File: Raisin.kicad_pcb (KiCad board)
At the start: 2 copper layers, 6 parts, among them U1 ATMEGA328P-AU, U10 L78L06_TO92, U5 LD1117S33TR_SOT223, U6 L78L05_TO92, U7 FSA3157L6X, U8 AD5171

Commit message: bad pcb layout
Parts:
- removed U8: AD5171, TO_SOT_Packages_SMD:SOT-23-8_Handsoldering
- added C1: 100nF, raisin:C_1206_0603, F.Cu at (102.5, 135.8)
- added C10: 10uF, Capacitors_ThroughHole:CP_Radial_D4.0mm_P2.00mm, B.Cu at (150.7, 99.7)
- added C11: 10nF, raisin:C_1206_0603, F.Cu at (76.9, 103.7)
- added C12: 10nF, raisin:C_1206_0603, F.Cu at (73.0, 79.8)
- added C13: 100nF, raisin:C_1206_0603, F.Cu at (75.5, 128.3)
- added C14: 10nF, raisin:C_1206_0603, F.Cu at (70.9, 110.0)
- added C15: 100nF, raisin:C_1206_0603, F.Cu at (83.4, 109.3)
- added C16: 10nF, raisin:C_1206_0603, F.Cu at (68.0, 95.9)
- added C17: 100nF, raisin:C_1206_0603, F.Cu at (68.2, 120.2)
- added C19: 100nF, raisin:C_1206_0603, F.Cu at (79.2, 120.3)
- added C2: 100nF, raisin:C_1206_0603, F.Cu at (108.5, 119.2)
- added C20: 220nF, raisin:C_1206_0603, F.Cu at (100.2, 102.6)
- added C21: 220nF, raisin:C_1206_0603, F.Cu at (105.3, 102.6)
- added C22: 220nF, raisin:C_1206_0603, F.Cu at (110.3, 102.6)
- added C23: 220nF, raisin:C_1206_0603, F.Cu at (115.4, 102.6)
- added C24: 10nF, raisin:C_1206_0603, F.Cu at (83.5, 86.7)
- added C25: 100nF, raisin:C_1206_0603, F.Cu at (80.0, 96.0)
- added C26: 220nF, raisin:C_1206_0603, F.Cu at (120.5, 102.6)
- added C27: 100nF, raisin:C_1206_0603, F.Cu at (79.2, 87.0)
- added C28: 220nF, raisin:C_1206_0603, F.Cu at (125.5, 102.6)
- added C29: 33uF, Capacitors_ThroughHole:CP_Radial_D6.3mm_P2.50mm, B.Cu at (85.0, 98.0)
- added C3: 22pF, raisin:C_1206_0603, F.Cu at (128.7, 132.4)
- added C30: 220nF, raisin:C_1206_0603, F.Cu at (130.6, 102.6)
- added C31: 100nF, raisin:C_1206_0603, F.Cu at (122.9, 76.5)
- added C32: 33uF, Capacitors_ThroughHole:CP_Radial_D6.3mm_P2.50mm, B.Cu at (125.2, 57.8)
- added C33: 100nF, raisin:C_1206_0603, F.Cu at (122.1, 56.5)
- added C34: 1uF, Capacitors_ThroughHole:CP_Radial_D4.0mm_P2.00mm, B.Cu at (134.3, 62.2)
- added C35: 100nF, raisin:C_1206_0603, F.Cu at (140.2, 97.0)
- added C36: 100nF, raisin:C_1206_0603, F.Cu at (117.2, 81.6)
- added C37: 75*, raisin:C_1206_0603, F.Cu at (125.8, 87.5)
- added C38: 100nF, raisin:C_1206_0603, F.Cu at (111.0, 91.6)
- added C39: 10nF, raisin:C_1206_0603, F.Cu at (85.4, 76.3)
- added C4: 22pF, raisin:C_1206_0603, F.Cu at (116.6, 132.4)
- added C40: 10nF, raisin:C_1206_0603, F.Cu at (130.7, 88.9)
- added C41: 10nF, raisin:C_1206_0603, F.Cu at (76.0, 52.9)
- added C42: 100nF, raisin:C_1206_0603, F.Cu at (112.4, 62.2)
- added C43: 1uF, Capacitors_ThroughHole:CP_Radial_D4.0mm_P2.00mm, B.Cu at (126.5, 48.1)
- added C44: 270, raisin:C_1206_0603, F.Cu at (68.8, 54.0)
- added C45: 27, raisin:C_1206_0603, F.Cu at (75.5, 59.0)
- added C46: 33, raisin:C_1206_0603, F.Cu at (69.5, 59.0)
- added C47: 100nF, raisin:C_1206_0603, F.Cu at (101.9, 70.3)
- added C48: 680, raisin:C_1206_0603, F.Cu at (66.8, 59.0)
- added C49: 100nF, raisin:C_1206_0603, F.Cu at (133.8, 77.8)
- added C5: 100nF, raisin:C_1206_0603, F.Cu at (116.8, 74.4)
- added C50: 10nF, raisin:C_1206_0603, F.Cu at (136.5, 83.2)
- added C51: 4n7, raisin:C_1206_0603, F.Cu at (119.1, 63.8)
- added C52: 10uF, Capacitors_ThroughHole:CP_Radial_D5.0mm_P2.50mm, B.Cu at (100.7, 67.1)
- added C53: 10nF, raisin:C_1206_0603, F.Cu at (133.8, 85.8)
- added C54: 47n, raisin:C_1206_0603, F.Cu at (112.5, 70.1)
- added C55: 100nF, raisin:C_1206_0603, F.Cu at (152.0, 61.7)
- added C56: 10nF, raisin:C_1206_0603, F.Cu at (150.9, 57.9)
- added C57: 10nF, raisin:C_1206_0603, F.Cu at (157.2, 57.9)
- added C58: 10uF, Capacitors_Tantalum_SMD:CP_Tantalum_Case-A_EIA-3216-18_Hand, F.Cu at (119.4, 76.1)
- added C59: 10nF, raisin:C_1206_0603, F.Cu at (138.6, 75.3)
- added C60: 100nF, raisin:C_1206_0603, F.Cu at (98.7, 112.5)
- added C61: 100nF, raisin:C_1206_0603, F.Cu at (149.5, 106.9)
- added C62: 10uF, Capacitors_ThroughHole:CP_Radial_D4.0mm_P2.00mm, B.Cu at (148.4, 111.8)
- added C63: 22, raisin:C_1206_0603, F.Cu at (78.0, 59.0)
- added C64: 27, raisin:C_1206_0603, F.Cu at (75.5, 67.4)
- added C65: 33, raisin:C_1206_0603, F.Cu at (69.5, 67.4)
- added C66: 680, raisin:C_1206_0603, F.Cu at (78.3, 67.4)
- added C67: 22, raisin:C_1206_0603, F.Cu at (66.8, 67.4)
- added C68: 27, raisin:C_1206_0603, F.Cu at (75.5, 75.6)
- added C69: 33, raisin:C_1206_0603, F.Cu at (69.5, 75.6)
- added C7: 22pF, raisin:C_1206_0603, F.Cu at (152.7, 84.7)
- added C70: 270, raisin:C_1206_0603, F.Cu at (66.8, 75.6)
- added C71: 1uF, Capacitors_ThroughHole:CP_Radial_D4.0mm_P2.00mm, B.Cu at (134.8, 70.0)
- added C72: 100nF, raisin:C_1206_0603, F.Cu at (89.9, 80.2)
- added C73: 33uF, Capacitors_ThroughHole:CP_Radial_D6.3mm_P2.50mm, B.Cu at (100.3, 80.8)
- added C74: 10nF, raisin:C_1206_0603, F.Cu at (106.5, 80.2)
- added C75: 10nF, raisin:C_1206_0603, F.Cu at (120.8, 89.2)
- added C76: 330uF, Capacitors_ThroughHole:CP_Radial_D8.0mm_P5.00mm, B.Cu at (110.7, 49.5)
- added C77: 100uF, Capacitors_ThroughHole:CP_Radial_D6.3mm_P2.50mm, B.Cu at (148.0, 121.5)
- added C78: 100pF, raisin:C_1206_0603, F.Cu at (103.2, 96.2)
- added C79: 100pF, raisin:C_1206_0603, F.Cu at (102.3, 109.0)
- added C8: 22pF, raisin:C_1206_0603, F.Cu at (146.6, 84.7)
- added C80: 100pF, raisin:C_1206_0603, F.Cu at (113.3, 96.2)
- added C81: 100pF, raisin:C_1206_0603, F.Cu at (112.5, 109.0)
- added C82: 100pF, raisin:C_1206_0603, F.Cu at (123.5, 96.2)
- added C83: 100pF, raisin:C_1206_0603, F.Cu at (122.5, 109.0)
- added C84: 100pF, raisin:C_1206_0603, F.Cu at (133.6, 96.2)
- added C9: 100nF, raisin:C_1206_0603, F.Cu at (154.0, 101.5)
- added CON1: AVR_ISP, Pin_Headers:Pin_Header_Straight_2x03_Pitch2.54mm, B.Cu at (118.3, 123.1)
- added D1: LL4148, Diodes_SMD:D_MiniMELF_Handsoldering, F.Cu at (72.5, 117.5)
- added D10: LL4148, Diodes_SMD:D_MiniMELF_Handsoldering, F.Cu at (132.1, 80.5)
- added D11: BB132, Diodes_SMD:D_SOD-323_HandSoldering, F.Cu at (105.3, 109.0)
- added D12: BB132, Diodes_SMD:D_SOD-323_HandSoldering, F.Cu at (110.3, 96.2)
- added D13: BB132, Diodes_SMD:D_SOD-323_HandSoldering, F.Cu at (115.4, 109.0)
- added D14: BB132, Diodes_SMD:D_SOD-323_HandSoldering, F.Cu at (120.5, 96.2)
- added D15: BB132, Diodes_SMD:D_SOD-323_HandSoldering, F.Cu at (125.5, 109.0)
- added D16: BB132, Diodes_SMD:D_SOD-323_HandSoldering, F.Cu at (130.6, 96.2)
- added D17: LL4148, Diodes_SMD:D_MiniMELF_Handsoldering, F.Cu at (113.5, 89.2)
- added D2: LL4148, Diodes_SMD:D_MiniMELF_Handsoldering, F.Cu at (95.0, 120.8)
- added D3: LL4148, Diodes_SMD:D_MiniMELF_Handsoldering, F.Cu at (75.0, 117.5)
- added D4: LL4148, Diodes_SMD:D_MiniMELF_Handsoldering, F.Cu at (125.7, 78.2)
- added D5: LL4148, Diodes_SMD:D_MiniMELF_Handsoldering, F.Cu at (118.7, 84.0)
- added D6: LL4148, Diodes_SMD:D_MiniMELF_Handsoldering, F.Cu at (119.9, 61.2)
- added D7: BAV99, TO_SOT_Packages_SMD:SOT-23_Handsoldering, F.Cu at (113.8, 57.9)
- added D8: LL4148, Diodes_SMD:D_MiniMELF_Handsoldering, F.Cu at (119.2, 91.6)
- added D9: BB132, Diodes_SMD:D_SOD-323_HandSoldering, F.Cu at (100.2, 96.2)
- added J1: PTT, Socket_Strips:Socket_Strip_Angled_1x02_Pitch2.54mm, B.Cu at (103.5, 142.5)
- added J10: Conn_01x05, Pin_Headers:Pin_Header_Straight_1x05_Pitch2.54mm, B.Cu at (108.8, 137.7)
- added J11: i2c, raisin:SSD1306, B.Cu at (142.5, 137.7)
- added J12: Barrel_Jack, Connect:BARREL_JACK, B.Cu at (103.1, 59.0)
- added J13: PA, Connectors_Molex:Molex_KK-41791-02_02x3.96mm_Straight, B.Cu at (92.4, 50.4)
- added J2: Line OUT, raisin:audio_jack_3_5mm_PJ307, B.Cu at (135.2, 48.5)
- added J3: MIC, raisin:audio_jack_3_5mm_PJ307, B.Cu at (147.7, 48.5)
- added J4: ANT_PA, raisin:RFCONNECTOR, B.Cu at (76.0, 50.4)
- added J5: Conn_01x01, Mounting_Holes:MountingHole_3.2mm_M3_DIN965_Pad, F.Cu at (85.0, 65.0)
- added J6: Conn_01x01, Mounting_Holes:MountingHole_3.2mm_M3_DIN965_Pad, F.Cu at (140.5, 65.0)
- added J7: Conn_01x01, Mounting_Holes:MountingHole_3.2mm_M3_DIN965_Pad, F.Cu at (140.5, 125.0)
- added J8: Conn_01x01, Mounting_Holes:MountingHole_3.2mm_M3_DIN965_Pad, F.Cu at (85.0, 125.0)
- added J9: KEY, raisin:audio_jack_3_5mm_PJ307, B.Cu at (75.5, 141.5)
- added L1: L_Small, raisin:Choke_Toroid_6,5x13mm_Vertical, B.Cu at (154.9, 76.9)
- added L10: 8.5uH, raisin:Choke_Toroid_6,5x13mm_Vertical, B.Cu at (66.1, 59.9)
- added L11: 8.5uH, raisin:Choke_Toroid_6,5x13mm_Vertical, B.Cu at (66.1, 68.3)
- added L2: 47uH, Resistors_ThroughHole:R_Axial_DIN0204_L3.6mm_D1.6mm_P7.62mm_Horizontal, B.Cu at (153.2, 105.9)
- added L3: 22uH, Resistors_ThroughHole:R_Axial_DIN0204_L3.6mm_D1.6mm_P7.62mm_Horizontal, B.Cu at (81.6, 100.0)
- added L4: 22uH, Resistors_ThroughHole:R_Axial_DIN0204_L3.6mm_D1.6mm_P7.62mm_Horizontal, B.Cu at (73.9, 103.2)
- added L5: 47uH, Resistors_ThroughHole:R_Axial_DIN0204_L3.6mm_D1.6mm_P7.62mm_Horizontal, B.Cu at (89.9, 83.6)
- added L6: 47uH, Resistors_ThroughHole:R_Axial_DIN0204_L3.6mm_D1.6mm_P7.62mm_Horizontal, B.Cu at (90.5, 67.1)
- added L7: 22uH, Resistors_ThroughHole:R_Axial_DIN0204_L3.6mm_D1.6mm_P7.62mm_Horizontal, B.Cu at (125.8, 84.0)
- added L8: 8.5uH, raisin:Choke_Toroid_6,5x13mm_Vertical, B.Cu at (66.1, 51.5)
- added Q1: MMBFJ310LT1G, TO_SOT_Packages_SMD:SOT-23_Handsoldering, F.Cu at (70.8, 104.7)
- added Q10: BSS138, TO_SOT_Packages_SMD:SOT-23_Handsoldering, F.Cu at (145.9, 58.0)
- added Q2: MMBFJ310LT1G, TO_SOT_Packages_SMD:SOT-23_Handsoldering, F.Cu at (76.9, 109.3)
- added Q3: Si2301-TP, TO_SOT_Packages_SMD:SOT-23_Handsoldering, F.Cu at (70.8, 128.2)
- added Q4: Si2301-TP, TO_SOT_Packages_SMD:SOT-23_Handsoldering, F.Cu at (73.5, 124.2)
- added Q5: 2N7002, TO_SOT_Packages_SMD:SOT-23_Handsoldering, F.Cu at (127.7, 65.6)
- added Q6: MMBT3906, TO_SOT_Packages_SMD:SOT-23_Handsoldering, F.Cu at (131.5, 65.6)
- added Q7: MMBFJ310LT1G, TO_SOT_Packages_SMD:SOT-23_Handsoldering, F.Cu at (135.3, 90.8)
- added Q8: 2N7002, TO_SOT_Packages_SMD:SOT-23_Handsoldering, F.Cu at (105.7, 88.1)
- added R1: 560, raisin:R_1206_0603, F.Cu at (120.9, 48.1)
- added R10: 10k, raisin:R_1206_0603, F.Cu at (79.9, 103.7)
- added R11: 2.7k, raisin:R_1206_0603, F.Cu at (78.1, 128.3)
- added R12: 2.7k, raisin:R_1206_0603, F.Cu at (80.7, 128.3)
- added R13: 10k, raisin:R_1206_0603, F.Cu at (67.5, 105.0)
- added R14: 30, raisin:R_1206_0603, F.Cu at (80.7, 109.3)
- added R15: 4.7k, raisin:R_1206_0603, F.Cu at (68.2, 123.2)
- added R16: 4.7k, raisin:R_1206_0603, F.Cu at (78.8, 123.1)
- added R17: 100, raisin:R_1206_0603, F.Cu at (86.2, 86.6)
- added R18: 100, raisin:R_1206_0603, F.Cu at (83.5, 91.2)
- added R19: 3,3k, raisin:R_1206_0603, F.Cu at (84.5, 95.0)
- added R2: 300k, raisin:R_1206_0603, F.Cu at (97.3, 96.2)
- added R20: 3,3k, raisin:R_1206_0603, F.Cu at (77.0, 96.0)
- added R21: 1k, raisin:R_1206_0603, F.Cu at (128.4, 73.8)
- added R22: 1M, raisin:R_1206_0603, F.Cu at (118.5, 56.6)
- added R23: 150k*, raisin:R_1206_0603, F.Cu at (135.3, 58.8)
- added R24: 30, raisin:R_1206_0603, F.Cu at (140.2, 94.3)
- added R25: 300*, raisin:R_1206_0603, F.Cu at (130.7, 91.9)
- added R26: 10k, raisin:R_1206_0603, F.Cu at (140.2, 91.8)
- added R27: 1k, raisin:R_1206_0603, F.Cu at (128.9, 84.4)
- added R28: 1k, raisin:R_1206_0603, F.Cu at (131.1, 73.9)
- added R29: 300k, raisin:R_1206_0603, F.Cu at (118.3, 109.0)
- added R3: 10k, raisin:R_1206_0603, F.Cu at (98.2, 131.5)
- added R30: 15k, raisin:R_1206_0603, F.Cu at (113.4, 66.5)
- added R31: 1k, raisin:R_1206_0603, B.Cu at (119.0, 72.0)
- added R32: 1k, raisin:R_1206_0603, F.Cu at (154.0, 57.9)
- added R33: 15k, raisin:R_1206_0603, F.Cu at (156.5, 53.5)
- added R34: 15k, raisin:R_1206_0603, F.Cu at (125.0, 70.4)
- added R35: 300*, raisin:R_1206_0603, F.Cu at (115.5, 78.1)
- added R36: 300k, raisin:R_1206_0603, F.Cu at (117.5, 96.2)
- added R37: 300k, raisin:R_1206_0603, F.Cu at (128.4, 109.0)
- added R38: 300k, raisin:R_1206_0603, F.Cu at (127.7, 96.2)
- added R39: 1k, raisin:R_1206_0603, F.Cu at (117.2, 86.6)
- added R4: 4.7k, raisin:R_1206_0603, F.Cu at (143.7, 141.2)
- added R40: 470k, raisin:R_1206_0603, F.Cu at (79.2, 132.9)
- added R41: 470k, raisin:R_1206_0603, F.Cu at (72.0, 132.9)
- added R42: 1k, raisin:R_1206_0603, F.Cu at (111.8, 117.2)
- added R5: 4.7k, raisin:R_1206_0603, F.Cu at (142.6, 134.7)
- added R6: 100, raisin:R_1206_0603, F.Cu at (112.5, 72.4)
- added R7: 300k, raisin:R_1206_0603, F.Cu at (108.2, 109.0)
- added R8: 300k, raisin:R_1206_0603, F.Cu at (107.5, 96.2)
- added R9: 30, raisin:R_1206_0603, F.Cu at (70.5, 100.0)
- added RV1: POT, raisin:Potentiometer_WH148, B.Cu at (95.1, 141.2)
- added RV2: POT, raisin:Potentiometer_Trimmer_Piher_PT-6v_Horizontal, B.Cu at (134.5, 125.0)
- added T1: 1:2, raisin:TF12, B.Cu at (70.5, 84.4)
- added T2: Transformer, raisin:TF14, B.Cu at (70.5, 89.8)
- added T3: Transformer, raisin:TF14, B.Cu at (86.0, 109.0)
- added T4: Transformer, raisin:TF14, B.Cu at (141.9, 102.7)
- added U2: Si5351, Housings_SSOP:MSOP-10_3x3mm_Pitch0.5mm, F.Cu at (101.7, 73.6)
- added U3: NE5532, Housings_SOIC:SOIC-8_3.9x4.9mm_Pitch1.27mm, F.Cu at (119.5, 68.0)
- added U4: SA612A, raisin:DIP-8_SOIC-8_W7.62mm, B.Cu at (152.1, 94.9)
- added Y1: 8Mhz, raisin:Crystal_HC49-U_Vertical, B.Cu at (125.1, 132.4)
- added Y10: Crystal_GND23_Small, raisin:Crystal_HC49-U_Vertical, B.Cu at (123.0, 105.0)
- added Y11: Crystal_GND23_Small, raisin:Crystal_HC49-U_Vertical, B.Cu at (128.0, 100.2)
- added Y12: Crystal_GND23_Small, raisin:Crystal_HC49-U_Vertical, B.Cu at (138.1, 105.0)
- added Y13: Crystal_GND23_Small, raisin:Crystal_HC49-U_Vertical, B.Cu at (133.1, 105.0)
- added Y2: 27Mhz, Crystals:Crystal_SMD_HC49-SD, F.Cu at (95.0, 77.5)
- added Y3: Crystal_GND23_Small, raisin:Crystal_HC49-U_Vertical, B.Cu at (146.2, 80.8)
- added Y4: Crystal_GND23_Small, raisin:Crystal_HC49-U_Vertical, B.Cu at (92.7, 100.2)
- added Y5: Crystal_GND23_Small, raisin:Crystal_HC49-U_Vertical, B.Cu at (97.7, 100.2)
- added Y6: Crystal_GND23_Small, raisin:Crystal_HC49-U_Vertical, B.Cu at (102.8, 105.0)
- added Y7: Crystal_GND23_Small, raisin:Crystal_HC49-U_Vertical, B.Cu at (107.8, 100.2)
- added Y8: Crystal_GND23_Small, raisin:Crystal_HC49-U_Vertical, B.Cu at (112.9, 105.0)
- added Y9: Crystal_GND23_Small, raisin:Crystal_HC49-U_Vertical, B.Cu at (117.9, 100.2)
- U10, U6: moved to B.Cu
- moved U7 70.6 mm to (79.3, 91.2)
- moved U6 57.5 mm to (94.1, 86.5), turned to 270 degrees
- moved U1 46.4 mm to (108.0, 127.8), turned to 90 degrees
- moved U5 17.4 mm to (154.0, 121.5), turned to 180 degrees
- moved U10 5.92 mm to (153.2, 108.5), turned to 270 degrees
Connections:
- U1 pad 1: (no net) -> Net-(J10-Pad2)
- U1 pad 10: (no net) -> Net-(R40-Pad2)
- U1 pad 13: (no net) -> Net-(J1-Pad1)
- U1 pad 14: (no net) -> TONE
- U1 pad 15: (no net) -> KEY
- U1 pad 16: (no net) -> PTT
- U1 pad 17: (no net) -> Net-(CON1-Pad3)
- U1 pad 19: (no net) -> Net-(J10-Pad3)
- U1 pad 2: (no net) -> Net-(J9-Pad2)
- U1 pad 20: (no net) -> Net-(C2-Pad2)
- U1 pad 22: (no net) -> Net-(RV2-Pad2)
- U1 pad 29: (no net) -> Net-(CON1-Pad5)
- U1 pad 32: (no net) -> Net-(J10-Pad1)
- U1 pad 7: (no net) -> Net-(C3-Pad1)
- U1 pad 8: (no net) -> Net-(C4-Pad1)
- U1 pad 9: (no net) -> Net-(J9-Pad1)
- U10 pad 1: (no net) -> Net-(C61-Pad1)
- U6 pad 1: (no net) -> Net-(C72-Pad1)
- U7 pad 1: (no net) -> Net-(T1-Pad3)
- U7 pad 3: (no net) -> Net-(T1-Pad4)
- U7 pad 4: (no net) -> Net-(C25-Pad1)
- U7 pad 5: (no net) -> Net-(C27-Pad1)
- U7 pad 6: (no net) -> Net-(C24-Pad1)
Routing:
- net SCL: track 0.00 -> 140.8 mm, vias 0 -> 1
- net SDA: track 0.00 -> 138.2 mm, vias 0 -> 1
- net Net-(C60-Pad1): track 0.00 -> 111.8 mm, vias 0 -> 2
- net RX: track 0.00 -> 52.8 mm, vias 0 -> 2
- net Net-(C42-Pad1): track 0.00 -> 38.1 mm
- net Net-(Q8-Pad1): track 0.00 -> 32.6 mm, vias 0 -> 2
- net Net-(C34-Pad1): track 0.00 -> 31.3 mm
- net Net-(C39-Pad1): track 0.00 -> 30.6 mm
- net Net-(C57-Pad1): track 0.00 -> 28.9 mm
- net Net-(C43-Pad1): track 0.00 -> 23.3 mm
- net Net-(C37-Pad1): track 0.00 -> 22.5 mm, vias 0 -> 2
- net AGC_OFF: track 0.00 -> 22.2 mm
- net Net-(C37-Pad2): track 0.00 -> 22.1 mm
- net Net-(C3-Pad1): track 0.00 -> 21.9 mm
- net Net-(C11-Pad2): track 0.00 -> 20.3 mm, vias 0 -> 1
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- added copper zone on B.Cu, net GND
- added copper zone on F.Cu, net GND
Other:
- board outline added: 95.5 x 100 mm

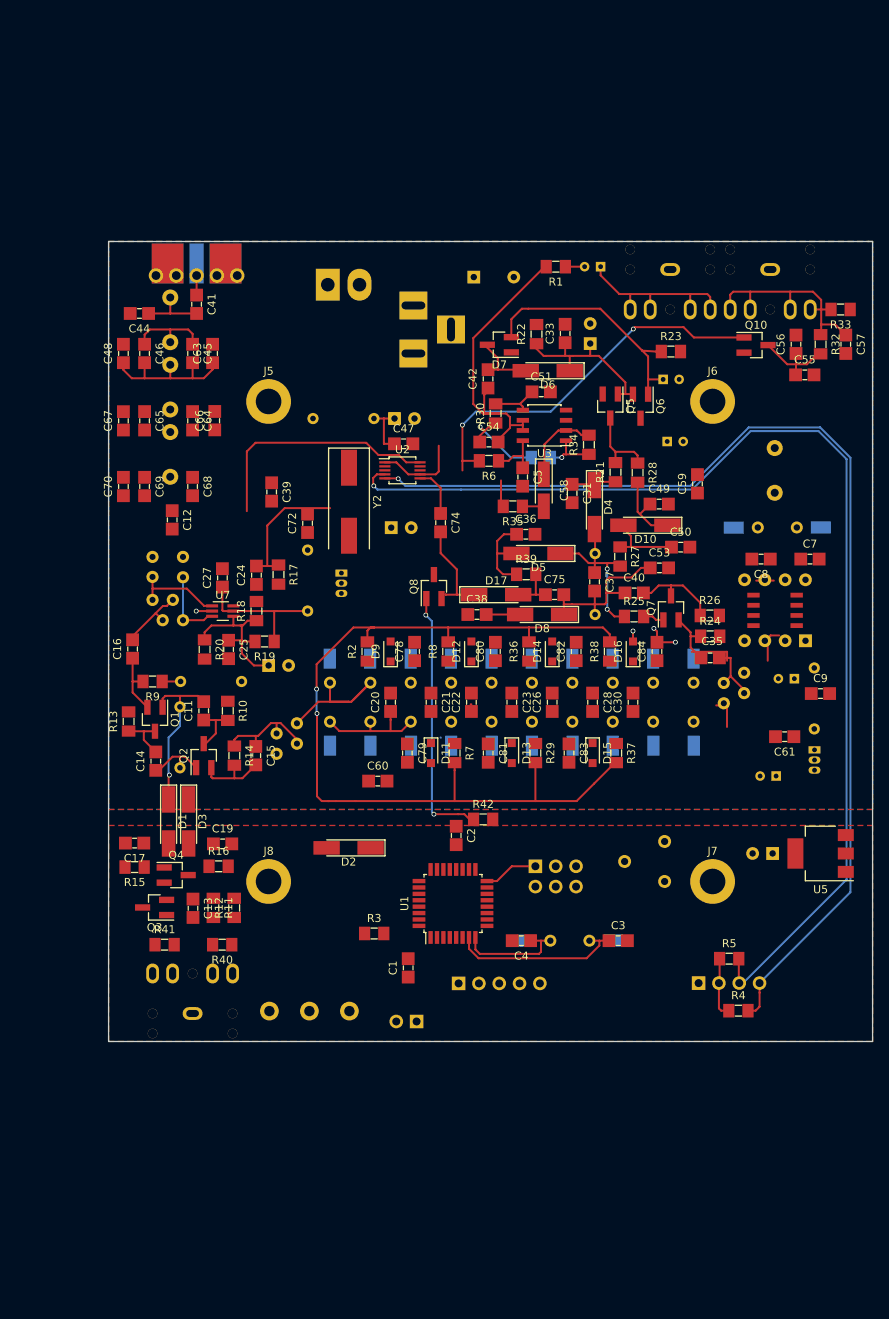
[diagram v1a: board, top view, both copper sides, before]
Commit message: PCB to 0603, Buzzer
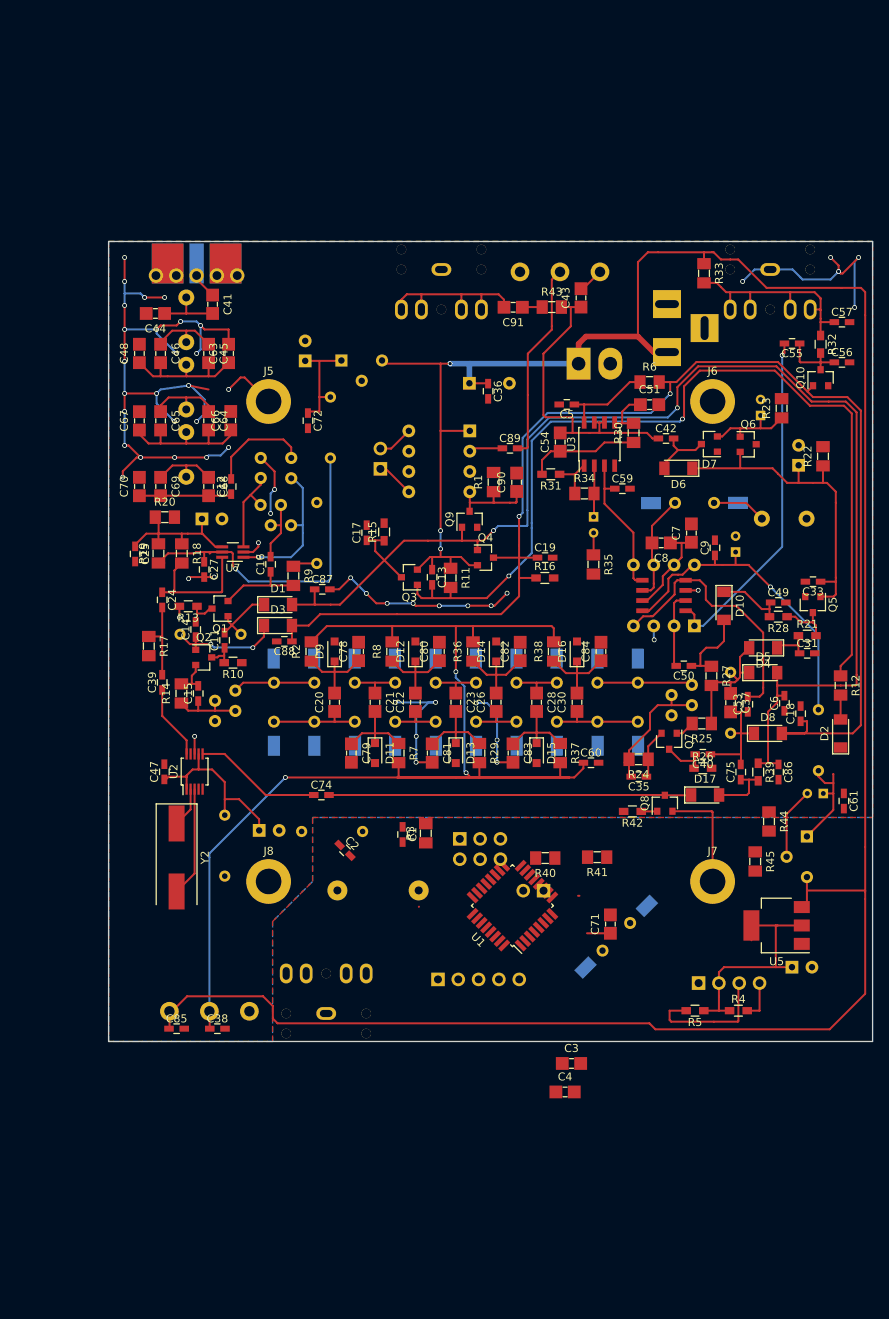
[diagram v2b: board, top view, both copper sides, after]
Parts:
- removed RV2: POT, raisin:Potentiometer_Trimmer_Piher_PT-6v_Horizontal
- added C18: 100nF, Capacitors_SMD:C_0603_HandSoldering, F.Cu at (151.5, 104.0)
- added C6: 100nF, Capacitors_SMD:C_0603_HandSoldering, F.Cu at (149.5, 102.7)
- added C85: 100nF, Capacitors_SMD:C_0603_HandSoldering, F.Cu at (73.5, 143.4)
- added C86: 100nF, Capacitors_SMD:C_0603_HandSoldering, F.Cu at (148.7, 111.3)
- added C87: 100nF, Capacitors_SMD:C_0603_HandSoldering, F.Cu at (91.7, 88.5)
- added C88: 100nF, Capacitors_SMD:C_0603_HandSoldering, F.Cu at (87.0, 95.0)
- added C89: 100nF, Capacitors_SMD:C_0603_HandSoldering, F.Cu at (115.2, 70.8)
- added C90: 1uF, raisin:C_1206_0603, F.Cu at (116.0, 75.1)
- added C91: 1uF, raisin:C_1206_0603, F.Cu at (115.6, 53.2)
- added J14: Conn_01x02, Pin_Headers:Pin_Header_Straight_1x02_Pitch2.54mm, B.Cu at (99.0, 73.4)
- added L9: 22uH, Resistors_ThroughHole:R_Axial_DIN0204_L3.6mm_D1.6mm_P7.62mm_Horizontal, B.Cu at (96.8, 118.8)
- added LS1: Speaker, Buzzers_Beepers:BUZZER, B.Cu at (98.7, 126.1)
- added Q9: 2N7002, TO_SOT_Packages_SMD:SOT-23, F.Cu at (110.1, 79.7)
- added R43: 100, raisin:R_1206_0603, F.Cu at (120.4, 53.2)
- added R44: 10k, raisin:R_1206_0603, F.Cu at (147.6, 117.5)
- added R45: 10k, raisin:R_1206_0603, F.Cu at (145.8, 122.5)
- added RV3: POT, raisin:Potentiometer_WH148, B.Cu at (116.4, 48.8)
- added U8: TDA7052A, Housings_DIP:DIP-8_W7.62mm, B.Cu at (110.2, 68.7)
- C1, C11, C12, C13, C14, C15, C16, C17, C19, C2, C24, C25, C27, C31, C33, C35, C36, C38, C39, C40, C42, C47, C49, C5, C50, C53, C55, C56, C57, C59, C60, C61, C72, C74, C75, C9: footprint raisin:C_1206_0603 -> Capacitors_SMD:C_0603_HandSoldering
- C43, C71: footprint Capacitors_ThroughHole:CP_Radial_D4.0mm_P2.00mm -> raisin:C_1206_0603; moved to F.Cu
- C58: footprint Capacitors_Tantalum_SMD:CP_Tantalum_Case-A_EIA-3216-18_Hand -> Capacitors_ThroughHole:CP_Radial_D4.0mm_P2.00mm; moved to B.Cu
- D1, D10, D17, D2, D3, D4, D5, D6, D8: footprint Diodes_SMD:D_MiniMELF_Handsoldering -> Diodes_SMD:D_MiniMELF
- D7, Q1, Q10, Q2, Q3, Q4, Q5, Q6, Q7, Q8: footprint TO_SOT_Packages_SMD:SOT-23_Handsoldering -> TO_SOT_Packages_SMD:SOT-23
- J1: value PTT -> CW_KEY; footprint Socket_Strips:Socket_Strip_Angled_1x02_Pitch2.54mm -> Pin_Headers:Pin_Header_Straight_1x02_Pitch2.54mm
- J9: value KEY -> PTT
- R1: value 560 -> 150k*
- R10, R13, R15, R16, R21, R26, R28, R32, R39, R4, R5: footprint raisin:R_1206_0603 -> Resistors_SMD:R_0603_HandSoldering
- R25: value 300* -> 15
- R27: value 1k -> 150
- R31: footprint raisin:R_1206_0603 -> Resistors_SMD:R_0603_HandSoldering; moved to F.Cu
- R42: value 1k -> 10k; footprint raisin:R_1206_0603 -> Resistors_SMD:R_0603_HandSoldering
- U10, U6: footprint TO_SOT_Packages_THT:TO-92_Inline_Narrow_Oval -> TO_SOT_Packages_THT:TO-92_Molded_Wide
- Y1: value 8Mhz -> Crystal_GND23_Small
- moved R12 80.7 mm to (156.5, 100.5), turned to 270 degrees
- moved D2 63.1 mm to (156.5, 106.5), turned to 90 degrees
- moved C38 61.1 mm to (78.6, 143.4)
- moved C71 60.7 mm to (127.7, 130.3), turned to 90 degrees
- moved L6 58.3 mm to (79.5, 124.3), turned to 90 degrees
- moved Q4 55.4 mm to (112.1, 84.5)
- moved R41 55.2 mm to (126.1, 122.0), turned to 180 degrees
- moved R16 54.4 mm to (119.5, 87.1)
- moved C52 54.2 mm to (83.8, 118.6)
- moved C19 53.9 mm to (119.6, 84.5)
- moved R15 52.2 mm to (99.4, 81.3), turned to 90 degrees
- moved Q3 52.1 mm to (102.6, 87.0)
- moved C13 51.0 mm to (105.4, 87.0)
- moved R11 50.8 mm to (107.8, 87.0)
- moved C47 50.8 mm to (72.0, 111.3), turned to 90 degrees
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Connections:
- net TONE renamed Net-(C71-Pad2)
- C1 pad 1: GND -> GNDD
- C2 pad 1: GND -> GNDD
- C3 pad 2: GND -> GNDD
- C36 pad 1: TX -> +12V
- C38 pad 1: GND -> Net-(C38-Pad1)
- C38 pad 2: RX -> GND
- C4 pad 2: GND -> GNDD
- C43 pad 1: Net-(C43-Pad1) -> Net-(C42-Pad1)
- C60 pad 1: Net-(C60-Pad1) -> Net-(C38-Pad1)
- C71 pad 1: Net-(C43-Pad1) -> Net-(C71-Pad1)
- C77 pad 2: GND -> GNDD
- CON1 pad 6: GND -> GNDD
- J1 pad 2: GND -> Net-(J1-Pad2)
- J11 pad 1: GND -> GNDD
- J2 pad 1: Net-(C43-Pad1) -> Net-(C91-Pad2)
- J2 pad 2: Net-(C43-Pad1) -> Net-(C91-Pad2)
- J2 pad 4: Net-(C43-Pad1) -> Net-(C91-Pad2)
- J2 pad 5: Net-(C43-Pad1) -> Net-(C91-Pad2)
- J9 pad 3: GND -> GNDD
- L6 pad 1: +3V3 -> (no net)
- R1 pad 1: Net-(C43-Pad2) -> Net-(C90-Pad1)
- R1 pad 2: Net-(C42-Pad1) -> GND
- R2 pad 2: Net-(C60-Pad1) -> Net-(C38-Pad1)
- R29 pad 2: Net-(C60-Pad1) -> Net-(C38-Pad1)
- R36 pad 2: Net-(C60-Pad1) -> Net-(C38-Pad1)
- R37 pad 2: Net-(C60-Pad1) -> Net-(C38-Pad1)
- R38 pad 2: Net-(C60-Pad1) -> Net-(C38-Pad1)
- R40 pad 1: Net-(J9-Pad2) -> Net-(J1-Pad1)
- R41 pad 1: Net-(J9-Pad1) -> Net-(J1-Pad2)
- R7 pad 2: Net-(C60-Pad1) -> Net-(C38-Pad1)
- R8 pad 2: Net-(C60-Pad1) -> Net-(C38-Pad1)
- RV1 pad 2: Net-(C60-Pad1) -> Net-(C38-Pad1)
- T1 pad 1: Net-(C12-Pad2) -> GND
- T1 pad 2: GND -> Net-(C12-Pad2)
- U1 pad 10: Net-(R40-Pad2) -> Net-(J1-Pad1)
- U1 pad 12: (no net) -> AGC_OFF
- U1 pad 13: Net-(J1-Pad1) -> (no net)
- U1 pad 19: Net-(J10-Pad3) -> Net-(R44-Pad2)
- U1 pad 2: Net-(J9-Pad2) -> Net-(R40-Pad2)
- U1 pad 21: GND -> GNDD
- U1 pad 22: Net-(RV2-Pad2) -> Net-(J10-Pad3)
- U1 pad 3: GND -> GNDD
- U1 pad 30: (no net) -> Net-(J9-Pad1)
- U1 pad 31: (no net) -> Net-(J9-Pad2)
- U1 pad 5: GND -> GNDD
- U1 pad 9: Net-(J9-Pad1) -> Net-(J1-Pad2)
- U5 pad 1: GND -> GNDD
- U7 pad 1: Net-(T1-Pad3) -> Net-(T1-Pad4)
- U7 pad 3: Net-(T1-Pad4) -> Net-(T1-Pad3)
- Y1 pad 1: Net-(C3-Pad1) -> Net-(C4-Pad1)
- Y1 pad 2: Net-(C4-Pad1) -> Net-(C3-Pad1)
- Y1 pad 3: GND -> GNDD
- Y1 pad 4: GND -> GNDD
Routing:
- net +12V: track 0.00 -> 319.1 mm, vias 0 -> 3
- net GND: track 14.5 -> 219.2 mm, vias 4 -> 54
- net Net-(C38-Pad1): track 0.00 -> 157.5 mm, vias 0 -> 3
- net TX: track 11.4 -> 165.5 mm, vias 0 -> 2
- net SDA: track 138.2 -> 4.90 mm, vias 1 -> 0
- net SCL: track 140.8 -> 16.7 mm, vias 1 -> 0
- net Net-(C13-Pad2): track 0.00 -> 116.5 mm, vias 0 -> 2
- net RX: track 52.8 -> 166.4 mm
- net Net-(C60-Pad1): track 111.8 -> 0.00 mm, vias 2 -> 0
- net Net-(C55-Pad2): track 0.00 -> 43.3 mm, vias 0 -> 1
- net Net-(C10-Pad1): track 0.00 -> 42.7 mm, vias 0 -> 1
- net Net-(C74-Pad2): track 12.3 -> 45.3 mm
- net Net-(C53-Pad2): track 0.00 -> 32.8 mm
- net Net-(Q8-Pad1): track 32.6 -> 2.01 mm, vias 2 -> 0
- net Net-(C27-Pad1): track 17.4 -> 43.9 mm, vias 0 -> 1
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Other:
- net class Default: clearance 0.2 -> 0.25
- rule trace_clearance: 0.2 -> 0.25

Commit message: Add GND connection points
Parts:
- removed R22: 1M, raisin:R_1206_0603
- added C92: 100nF, Capacitors_SMD:C_0603_HandSoldering, F.Cu at (105.7, 129.3)
- added C93: 100nF, Capacitors_SMD:C_0603_HandSoldering, F.Cu at (107.5, 140.7)
- added C94: 100nF, Capacitors_SMD:C_0603_HandSoldering, F.Cu at (115.3, 140.0)
- added J15: TX, Pin_Headers:Pin_Header_Straight_1x02_Pitch2.54mm, B.Cu at (102.5, 80.0)
- added Q11: 2N7002, TO_SOT_Packages_SMD:SOT-23, F.Cu at (145.6, 117.9)
- added R46: 10k, raisin:R_1206_0603, F.Cu at (103.6, 131.3)
- added R47: 0*, raisin:R_1206_0603, F.Cu at (97.2, 112.6)
- J10: value Conn_01x05 -> Encoder; footprint Pin_Headers:Pin_Header_Straight_1x05_Pitch2.54mm -> raisin:Encoder_DY-40
- R3: footprint raisin:R_1206_0603 -> Resistors_SMD:R_0603_HandSoldering; moved to B.Cu
- R44, R45: value 10k -> 470k
- moved R45 45.8 mm to (100.0, 122.1), turned to 180 degrees
- moved R44 42.5 mm to (105.1, 120.1)
- moved C71 28.2 mm to (99.8, 126.1), turned to 180 degrees
- moved C1 25.5 mm to (121.2, 135.7), turned to 135 degrees
- moved C4 24.2 mm to (133.9, 130.2)
- moved C3 16.0 mm to (130.5, 133.6)
- moved J10 14.9 mm to (120.3, 142.0), turned to 90 degrees
- moved C2 14.0 mm to (107.7, 125.7)
- moved L9 13.6 mm to (90.0, 130.5)
- moved J1 11.9 mm to (131.2, 124.3), turned to 270 degrees
- moved R40 10.5 mm to (130.1, 121.8)
- moved R41 8.63 mm to (134.7, 121.8)
- moved R3 6.78 mm to (111.4, 119.7)
- moved C17 6.43 mm to (98.3, 87.8), turned to 180 degrees
- moved CON1 4.80 mm to (113.5, 118.5)
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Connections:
- net Net-(R44-Pad2) renamed S
- C32 pad 1: AGC_OFF -> Net-(C32-Pad1)
- C33 pad 1: AGC_OFF -> Net-(C32-Pad1)
- C60 pad 1: Net-(C38-Pad1) -> Net-(C60-Pad1)
- D6 pad 1: AGC_OFF -> Net-(C32-Pad1)
- J10 pad 1: Net-(J10-Pad1) -> GNDD
- J10 pad 2: Net-(J10-Pad2) -> +3V3
- J10 pad 4: (no net) -> Net-(C94-Pad1)
- J10 pad 5: (no net) -> Net-(C93-Pad1)
- L6 pad 1: (no net) -> +3V3
- Q5 pad 1: AGC_OFF -> Net-(C32-Pad1)
- Q6 pad 2: AGC_OFF -> Net-(C32-Pad1)
- R2 pad 2: Net-(C38-Pad1) -> Net-(C60-Pad1)
- R29 pad 2: Net-(C38-Pad1) -> Net-(C60-Pad1)
- R36 pad 2: Net-(C38-Pad1) -> Net-(C60-Pad1)
- R37 pad 2: Net-(C38-Pad1) -> Net-(C60-Pad1)
- R38 pad 2: Net-(C38-Pad1) -> Net-(C60-Pad1)
- R44 pad 1: AGC_OFF -> Net-(C32-Pad1)
- R7 pad 2: Net-(C38-Pad1) -> Net-(C60-Pad1)
- R8 pad 2: Net-(C38-Pad1) -> Net-(C60-Pad1)
- U1 pad 1: Net-(J10-Pad2) -> Net-(C94-Pad1)
- U1 pad 11: (no net) -> Net-(R40-Pad2)
- U1 pad 2: Net-(R40-Pad2) -> (no net)
- U1 pad 30: Net-(J9-Pad1) -> Net-(J9-Pad2)
- U1 pad 31: Net-(J9-Pad2) -> Net-(J9-Pad1)
- U1 pad 32: Net-(J10-Pad1) -> Net-(C93-Pad1)
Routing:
- net GND: track 219.2 -> 798.9 mm, vias 54 -> 191
- net GNDD: track 0.00 -> 188.0 mm, vias 0 -> 42
- net Net-(C38-Pad1): track 157.5 -> 41.2 mm, vias 3 -> 1
- net Net-(C32-Pad1): track 0.00 -> 116.0 mm, vias 0 -> 2
- net SDA: track 4.90 -> 101.3 mm, vias 0 -> 2
- net +3V3: track 30.7 -> 124.3 mm, vias 0 -> 1
- net Net-(C60-Pad1): track 0.00 -> 89.4 mm, vias 0 -> 2
- net SCL: track 16.7 -> 97.6 mm, vias 0 -> 2
- net PTT: track 0.00 -> 58.6 mm
- net Net-(CON1-Pad5): track 0.00 -> 32.0 mm, vias 0 -> 1
- net Net-(J9-Pad1): track 0.00 -> 31.7 mm
- net Net-(C92-Pad1): track 0.00 -> 24.9 mm, vias 0 -> 1
- net Net-(J1-Pad2): track 0.00 -> 23.4 mm
- net KEY: track 0.00 -> 23.4 mm
- net Net-(C71-Pad2): track 0.00 -> 21.1 mm, vias 0 -> 2
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- added copper zone on B.Cu, net GNDD
- added copper zone on F.Cu, net GNDD
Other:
- net class Default: clearance 0.25 -> 0.2
- rule trace_clearance: 0.25 -> 0.2
